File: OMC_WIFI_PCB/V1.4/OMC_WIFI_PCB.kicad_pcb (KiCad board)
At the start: 2 copper layers, 106.8 x 66 mm, 23 parts, among them J1 Conn_01x02_Male, J2 Conn_01x02_Female, J3 Conn_01x02_Male, J4 Switch, J5 Pins_FT232R, J6 Level shifter, J8 Regulador, K1 SLA-12VDC-SL-C, Q1 2N3904, U1 ESP32-WROOM-32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

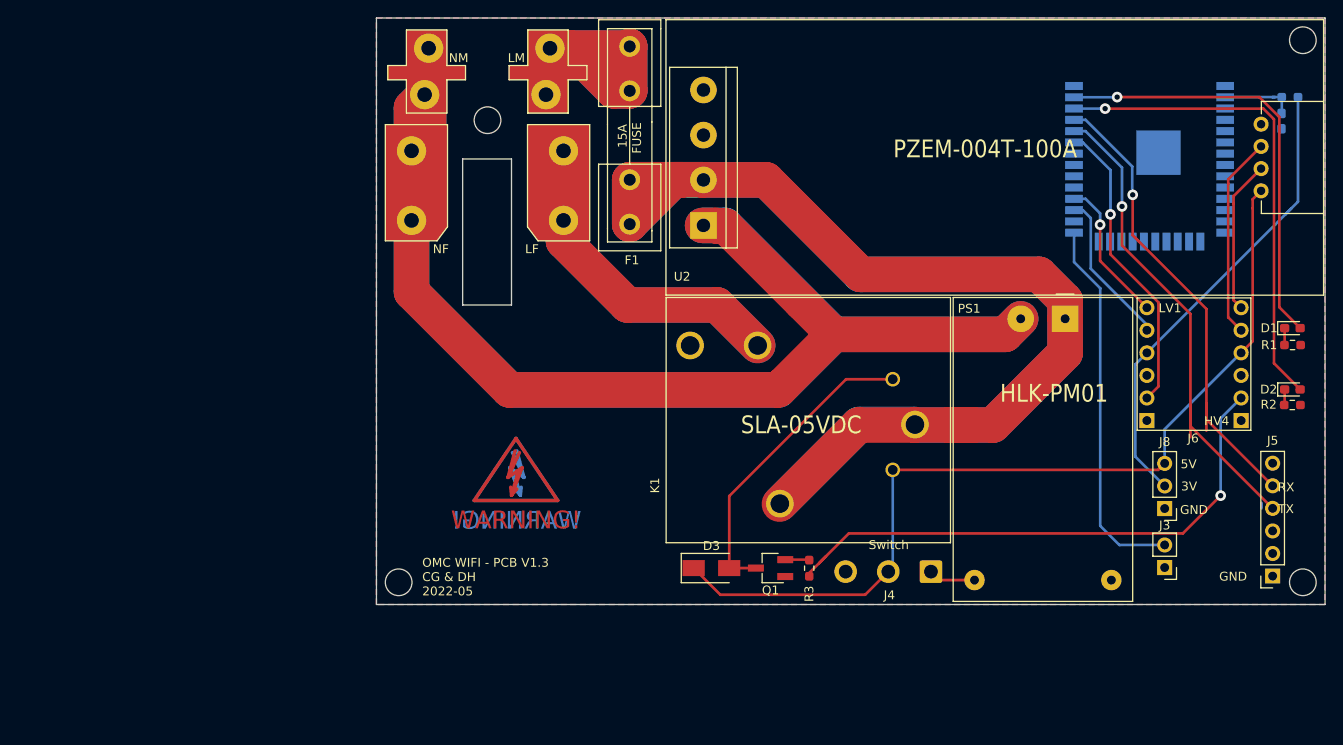
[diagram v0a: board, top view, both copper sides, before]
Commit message: Creación de versión 1.4 PCB
> Cambio en diseño para paso de cable por toroide.
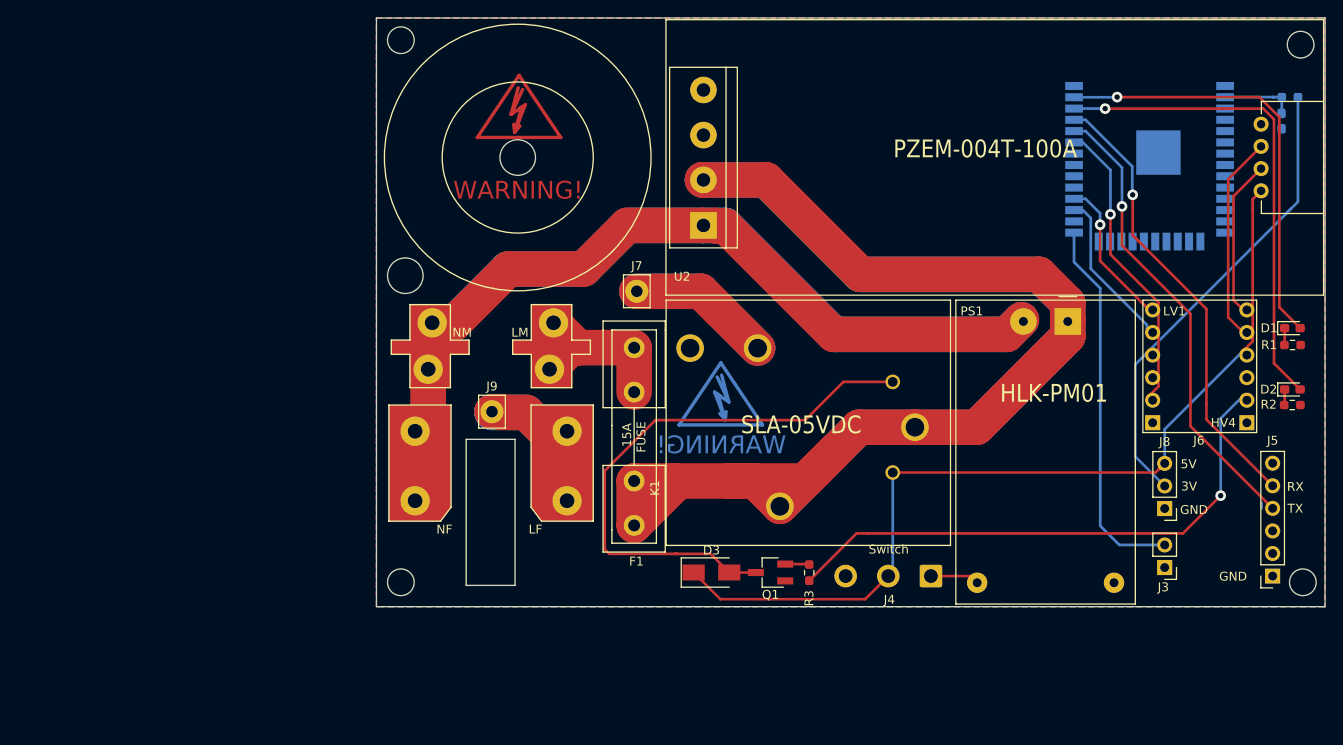
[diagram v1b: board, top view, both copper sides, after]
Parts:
- added J7: Conn_01x01_Female, Connector_Pin:Pin_D1.3mm_L10.0mm_W3.5mm_Flat, F.Cu at (605.3, -950.8)
- added J9: Conn_01x01_Female, Connector_Pin:Pin_D1.3mm_L10.0mm_W3.5mm_Flat, F.Cu at (589.0, -937.2)
- moved SYM1 40.9 mm to (592.0, -970.9)
- moved F1 33.9 mm to (605.0, -924.4)
- moved J2 31.6 mm to (588.9, -932.2)
- moved J1 30.9 mm to (582.0, -944.3)
- moved SYM2 24.6 mm to (614.8, -938.5)
- moved J6 0.70 mm to (668.6, -942.1)
- moved D3 0.50 mm to (613.7, -919.1)
- moved J4 0.50 mm to (638.4, -918.7)
- moved Q1 0.50 mm to (620.4, -919.1)
- moved R3 0.50 mm to (624.7, -919.1)
- moved PS1 0.42 mm to (653.8, -947.4)
- moved K1 0.30 mm to (618.9, -935.5)
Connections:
- J2 pad 2: LINE_OUT -> Net-(J2-Pad2)
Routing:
- net NEUTRAL: track 258.5 -> 168.6 mm
- net Net-(D3-Pad2): track 34.9 -> 63.8 mm
- net Net-(F1-Pad2): track 47.7 -> 19.5 mm
- net Net-(J2-Pad2): track 0.00 -> 25.4 mm
- net LINE_OUT: track 58.1 -> 34.6 mm
- net RX0: track 56.7 -> 53.1 mm
- net TX0: track 54.9 -> 51.8 mm
- net LINE_IN: track 230.4 -> 228.8 mm
- net Net-(J4-Pad1): track 5.29 -> 6.85 mm
- net +5V: track 101.9 -> 103.1 mm
- net D32_RELAY_5V: track 63.3 -> 62.6 mm
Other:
- board size 106.8 x 66 mm -> 106.8 x 66.2 mm
- board text added: "OMC WIFI - PCB V1.4 CG & DH 2022-05"
- board text removed: "OMC WIFI - PCB V1.3 CG & DH 2022-05"

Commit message: Primer código pruebas PZEM
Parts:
- added J10: Conn_01x01_Male, Connector_PinHeader_2.54mm:PinHeader_1x01_P2.54mm_Vertical, F.Cu at (679.2, -953.3)
- J4: footprint Connector_Wire:SolderWire-0.75sqmm_1x03_P4.8mm_D1.25mm_OD2.3mm -> Connector_PinHeader_2.54mm:PinHeader_1x03_P2.54mm_Vertical
- moved J4 7.15 mm to (631.2, -918.9), turned to 90 degrees
- moved J1 0.65 mm to (582.0, -944.9)
- moved J2 0.65 mm to (588.9, -932.9)
- moved J9 0.65 mm to (589.0, -937.9)
- moved SYM2 0.64 mm to (614.4, -939.0)
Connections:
- J4 pad 1: Net-(J4-Pad1) -> GND
- J4 pad 3: GND -> Net-(J4-Pad3)
- PS1 pad 4: Net-(J4-Pad1) -> Net-(J4-Pad3)
- U1 pad 8: Net-(U1-Pad8) -> TOUCH
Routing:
- net Net-(F1-Pad2): track 19.5 -> 77.2 mm
- net LINE_IN: track 228.8 -> 278.2 mm
- net TOUCH: track 0.00 -> 21.9 mm, vias 0 -> 2
- net NEUTRAL: track 168.6 -> 181.3 mm
- net Net-(J4-Pad3): track 0.00 -> 7.66 mm
- net Net-(J4-Pad1): track 6.85 -> 0.00 mm
- net TX0: track 51.8 -> 53.0 mm
- net RX2_3V: track 17.5 -> 18.6 mm
- net RX0: track 53.1 -> 52.5 mm
- net TX2_5V: track 22.8 -> 23.4 mm
- net D32_RELAY_3V: track 33.8 -> 34.3 mm
- net TX2_3V: track 16.4 -> 16.9 mm
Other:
- outline, holes or cut-outs redrawn
- board text added: "CT1"

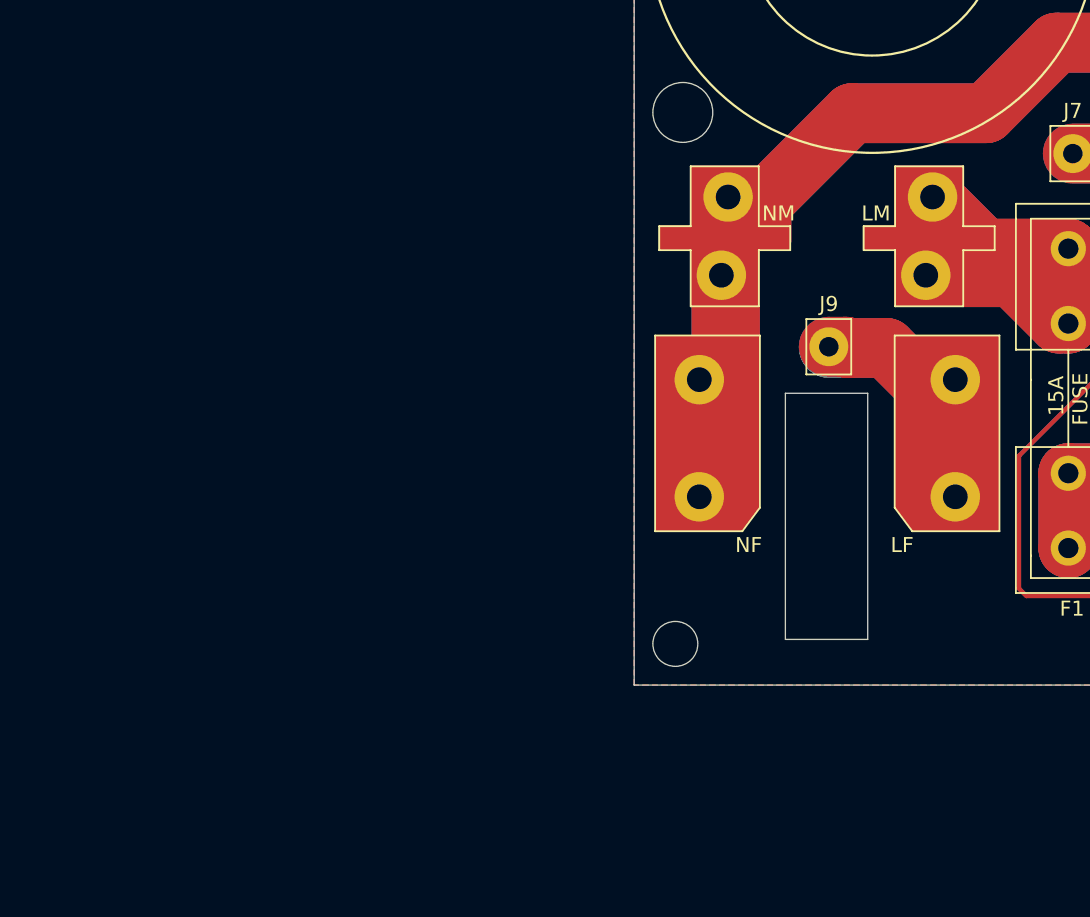
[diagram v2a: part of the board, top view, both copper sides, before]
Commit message: Creación de nuevas librerías conectores AC
Creación de librería 2D para conectores macho y hembra para AC
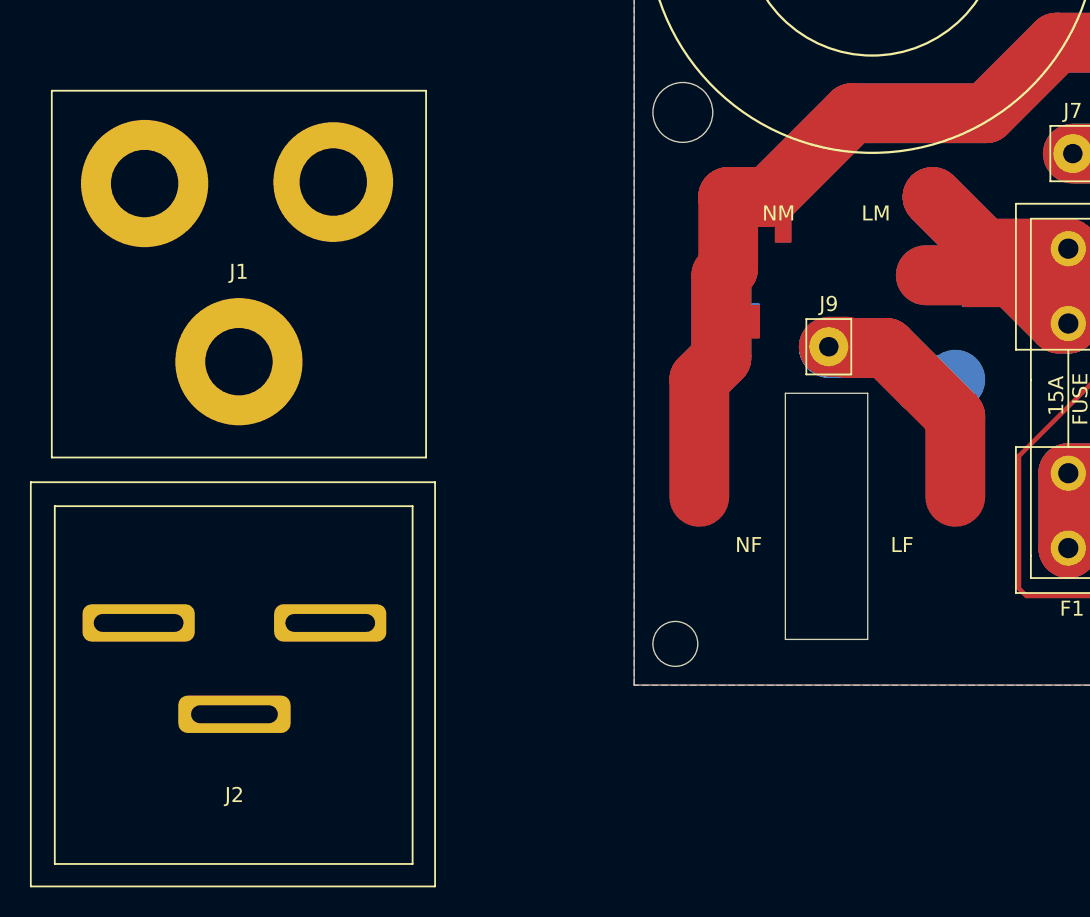
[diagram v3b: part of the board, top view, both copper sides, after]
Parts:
- J1: footprint omc-plugs:OMC-Male-Plug -> NEMA_5_P:NEMA_5_P
- J2: footprint omc-schematics LE:OMC-Female-Plug -> NEMA_5_R:NEMA_5_R
- moved J2 41.8 mm to (549.3, -919.4)
- moved J1 32.6 mm to (549.6, -948.8)
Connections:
- J1 pad 1: NEUTRAL -> Net-(F1-Pad2)
- J1 pad 2: Net-(F1-Pad2) -> NEUTRAL
- J2 pad 1: NEUTRAL -> Net-(J2-Pad1)
- J2 pad 2: Net-(J2-Pad2) -> NEUTRAL
- J9 pad 1: Net-(J2-Pad2) -> Net-(J2-Pad1)
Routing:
- net Net-(J2-Pad2): track 25.4 -> 0.00 mm
- net Net-(J2-Pad1): track 0.00 -> 25.4 mm
